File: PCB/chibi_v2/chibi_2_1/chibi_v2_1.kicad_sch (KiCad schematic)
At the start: 12 parts, among them J2 Conn_01x08_Pin, Q1 NPN, Q2 NPN, Q3 NPN

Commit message: PCB update, clearance issues solved (?)
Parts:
- renumbered Display to Display1, Pico to Pico1, SDCard to SDCard1
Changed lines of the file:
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@@
   (symbol (lib_id "components:Adafruit_Micro_SD_SPI_or_SDIO_Card_Breakout_Board") (at 161.29 60.96 0) (unit 1)
     (in_bom yes) (on_board yes) (dnp no) (fields_autoplaced)
-    (property "Reference" "SDCard" (at 184.15 43.18 0)
+    (property "Reference" "SDCard1" (at 184.15 43.18 0)
       (effects (font (size 1.27 1.27)) (justify left))
     )
@@
     (pin "1")
     (instances
-      (project "chibi_v2"
-        (path "/689cf35d-b2ef-4d92-8c34-285453c7ccd9"
-          (reference "SDCard") (unit 1)
+      (project "chibi_v2_1"
+        (path "/689cf35d-b2ef-4d92-8c34-285453c7ccd9"
+          (reference "SDCard1") (unit 1)
         )
       )
@@
     (pin "3")
     (instances
-      (project "chibi_v2"
+      (project "chibi_v2_1"
         (path "/689cf35d-b2ef-4d92-8c34-285453c7ccd9"
           (reference "Q2") (unit 1)
@@
     (pin "1")
     (instances
-      (project "chibi_v2"
+      (project "chibi_v2_1"
         (path "/689cf35d-b2ef-4d92-8c34-285453c7ccd9"
           (reference "#PWR010") (unit 1)
@@
     (pin "2")
     (instances
-      (project "chibi_v2"
+      (project "chibi_v2_1"
         (path "/689cf35d-b2ef-4d92-8c34-285453c7ccd9"
           (reference "R1") (unit 1)
@@
     (pin "1")
     (instances
-      (project "chibi_v2"
+      (project "chibi_v2_1"
         (path "/689cf35d-b2ef-4d92-8c34-285453c7ccd9"
           (reference "#PWR016") (unit 1)
@@
   (symbol (lib_id "SSD1306-128x64_OLED:SSD1306") (at 59.69 74.93 0) (unit 1)
     (in_bom yes) (on_board yes) (dnp no)
-    (property "Reference" "Display" (at 48.26 78.74 90)
+    (property "Reference" "Display1" (at 48.26 78.74 90)
       (effects (font (size 1.27 1.27)) (justify left))
     )
@@
     (pin "2")
     (instances
-      (project "chibi_v2"
-        (path "/689cf35d-b2ef-4d92-8c34-285453c7ccd9"
-          (reference "Display") (unit 1)
+      (project "chibi_v2_1"
+        (path "/689cf35d-b2ef-4d92-8c34-285453c7ccd9"
+          (reference "Display1") (unit 1)
         )
       )
@@
     (pin "2")
     (instances
-      (project "chibi_v2"
+      (project "chibi_v2_1"
         (path "/689cf35d-b2ef-4d92-8c34-285453c7ccd9"
           (reference "R2") (unit 1)
@@
     (pin "1")
     (instances
-      (project "chibi_v2"
+      (project "chibi_v2_1"
         (path "/689cf35d-b2ef-4d92-8c34-285453c7ccd9"
           (reference "#PWR07") (unit 1)
@@
     (pin "3")
     (instances
-      (project "chibi_v2"
+      (project "chibi_v2_1"
         (path "/689cf35d-b2ef-4d92-8c34-285453c7ccd9"
           (reference "Q1") (unit 1)
@@
     (pin "3")
     (instances
-      (project "chibi_v2"
+      (project "chibi_v2_1"
         (path "/689cf35d-b2ef-4d92-8c34-285453c7ccd9"
           (reference "J2") (unit 1)
@@
     (pin "1")
     (instances
-      (project "chibi_v2"
+      (project "chibi_v2_1"
         (path "/689cf35d-b2ef-4d92-8c34-285453c7ccd9"
           (reference "#PWR015") (unit 1)
@@
     (pin "1")
     (instances
-      (project "chibi_v2"
+      (project "chibi_v2_1"
         (path "/689cf35d-b2ef-4d92-8c34-285453c7ccd9"
           (reference "#PWR017") (unit 1)
@@
     (pin "1")
     (instances
-      (project "chibi_v2"
+      (project "chibi_v2_1"
         (path "/689cf35d-b2ef-4d92-8c34-285453c7ccd9"
           (reference "#PWR03") (unit 1)
@@
     (pin "2")
     (instances
-      (project "chibi_v2"
+      (project "chibi_v2_1"
         (path "/689cf35d-b2ef-4d92-8c34-285453c7ccd9"
           (reference "BZ1") (unit 1)
@@
   (symbol (lib_id "MCU_RaspberryPi_and_Boards:Pico") (at 113.03 86.36 0) (unit 1)
     (in_bom yes) (on_board yes) (dnp no) (fields_autoplaced)
-    (property "Reference" "Pico" (at 113.03 54.61 0)
+    (property "Reference" "Pico1" (at 113.03 54.61 0)
       (effects (font (size 1.27 1.27)))
     )
@@
     (pin "17")
     (instances
-      (project "chibi_v2"
-        (path "/689cf35d-b2ef-4d92-8c34-285453c7ccd9"
-          (reference "Pico") (unit 1)
+      (project "chibi_v2_1"
+        (path "/689cf35d-b2ef-4d92-8c34-285453c7ccd9"
+          (reference "Pico1") (unit 1)
         )
       )
@@
     (pin "1")
     (instances
-      (project "chibi_v2"
+      (project "chibi_v2_1"
         (path "/689cf35d-b2ef-4d92-8c34-285453c7ccd9"
           (reference "#PWR014") (unit 1)
@@
     (pin "1")
     (instances
-      (project "chibi_v2"
+      (project "chibi_v2_1"
         (path "/689cf35d-b2ef-4d92-8c34-285453c7ccd9"
           (reference "#PWR012") (unit 1)
@@
     (pin "1")
     (instances
-      (project "chibi_v2"
+      (project "chibi_v2_1"
         (path "/689cf35d-b2ef-4d92-8c34-285453c7ccd9"
           (reference "#PWR06") (unit 1)
@@
     (pin "1")
     (instances
-      (project "chibi_v2"
+      (project "chibi_v2_1"
         (path "/689cf35d-b2ef-4d92-8c34-285453c7ccd9"
           (reference "#PWR04") (unit 1)
@@
     (pin "1")
     (instances
-      (project "chibi_v2"
+      (project "chibi_v2_1"
         (path "/689cf35d-b2ef-4d92-8c34-285453c7ccd9"
           (reference "#PWR01") (unit 1)
@@
     (pin "1")
     (instances
-      (project "chibi_v2"
+      (project "chibi_v2_1"
         (path "/689cf35d-b2ef-4d92-8c34-285453c7ccd9"
           (reference "#PWR05") (unit 1)
@@
     (pin "1")
     (instances
-      (project "chibi_v2"
+      (project "chibi_v2_1"
         (path "/689cf35d-b2ef-4d92-8c34-285453c7ccd9"
           (reference "#PWR08") (unit 1)
@@
     (pin "2")
     (instances
-      (project "chibi_v2"
+      (project "chibi_v2_1"
         (path "/689cf35d-b2ef-4d92-8c34-285453c7ccd9"
           (reference "D1") (unit 1)
@@
     (pin "1")
     (instances
-      (project "chibi_v2"
+      (project "chibi_v2_1"
         (path "/689cf35d-b2ef-4d92-8c34-285453c7ccd9"
           (reference "#PWR013") (unit 1)
@@
     (pin "1")
     (instances
-      (project "chibi_v2"
+      (project "chibi_v2_1"
         (path "/689cf35d-b2ef-4d92-8c34-285453c7ccd9"
           (reference "#PWR011") (unit 1)
@@
     (pin "1")
     (instances
-      (project "chibi_v2"
+      (project "chibi_v2_1"
         (path "/689cf35d-b2ef-4d92-8c34-285453c7ccd9"
           (reference "#PWR09") (unit 1)
@@
     (pin "1")
     (instances
-      (project "chibi_v2"
+      (project "chibi_v2_1"
         (path "/689cf35d-b2ef-4d92-8c34-285453c7ccd9"
           (reference "#PWR02") (unit 1)
@@
     (pin "2")
     (instances
-      (project "chibi_v2"
+      (project "chibi_v2_1"
         (path "/689cf35d-b2ef-4d92-8c34-285453c7ccd9"
           (reference "D2") (unit 1)
@@
     (pin "3")
     (instances
-      (project "chibi_v2"
+      (project "chibi_v2_1"
         (path "/689cf35d-b2ef-4d92-8c34-285453c7ccd9"
           (reference "Q3") (unit 1)

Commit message: charging pins, grb + drl files added
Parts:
- added J1: Conn_01x02, Connector_PinHeader_2.54mm:PinHeader_1x02_P2.54mm_Vertical, symbol Connector_Generic:Conn_01x02
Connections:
- net GND: now also J1.1 (Pin_1)
- net at Pico1.40 (VBUS): now also J1.2 (Pin_2)
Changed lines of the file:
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@@
+    (stroke (width 0) (type default))
+  )
+  (wire (pts (xy 134.62 64.77) (xy 143.51 64.77))
     (stroke (width 0) (type default))
   )
@@
     (stroke (width 0) (type default))
   )
+  (wire (pts (xy 130.81 62.23) (xy 134.62 62.23))
+    (stroke (width 0) (type default))
+  )
   (wire (pts (xy 74.93 74.93) (xy 95.25 74.93))
     (stroke (width 0) (type default))
@@
   )
   (wire (pts (xy 87.63 60.96) (xy 87.63 64.77))
+    (stroke (width 0) (type default))
+  )
+  (wire (pts (xy 134.62 62.23) (xy 134.62 64.77))
     (stroke (width 0) (type default))
   )
@@
     )
   )
+  (symbol (lib_id "Connector_Generic:Conn_01x02") (at 148.59 62.23 0) (unit 1)
+    (in_bom yes) (on_board yes) (dnp no) (fields_autoplaced)
+    (property "Reference" "J1" (at 151.13 62.23 0)
+      (effects (font (size 1.27 1.27)) (justify left))
+    )
+    (property "Value" "Conn_01x02" (at 151.13 64.77 0)
+      (effects (font (size 1.27 1.27)) (justify left))
+    )
+    (property "Footprint" "Connector_PinHeader_2.54mm:PinHeader_1x02_P2.54mm_Vertical" (at 148.59 62.23 0)
+      (effects (font (size 1.27 1.27)) hide)
+    )
+    (property "Datasheet" "~" (at 148.59 62.23 0)
+      (effects (font (size 1.27 1.27)) hide)
+    )
+    (pin "1")
+    (pin "2")
+    (instances
+      (project "chibi_v2_1"
+        (path "/689cf35d-b2ef-4d92-8c34-285453c7ccd9"
+          (reference "J1") (unit 1)
+        )
+      )
+    )
+  )
   (symbol (lib_id "Device:LED") (at 81.28 115.57 180) (unit 1)
     (in_bom yes) (on_board yes) (dnp no) (fields_autoplaced)
@@
         )
       )
+    )
+  )
+  (symbol (lib_id "power:GND") (at 143.51 62.23 270) (unit 1)
+    (in_bom yes) (on_board yes) (dnp no) (fields_autoplaced)
+    (property "Reference" "#PWR018" (at 137.16 62.23 0)
+      (effects (font (size 1.27 1.27)) hide)
+    )
+    (property "Value" "GND" (at 139.7 62.23 90)
+      (effects (font (size 1.27 1.27)) (justify right))
+    )
+    (property "Footprint" "" (at 143.51 62.23 0)
+      (effects (font (size 1.27 1.27)) hide)
+    )
+    (property "Datasheet" "" (at 143.51 62.23 0)
+      (effects (font (size 1.27 1.27)) hide)
+    )
+    (pin "1")
+    (instances
+      (project "chibi_v2_1"
+        (path "/689cf35d-b2ef-4d92-8c34-285453c7ccd9"
+          (reference "#PWR018") (unit 1)
+        )
+      )

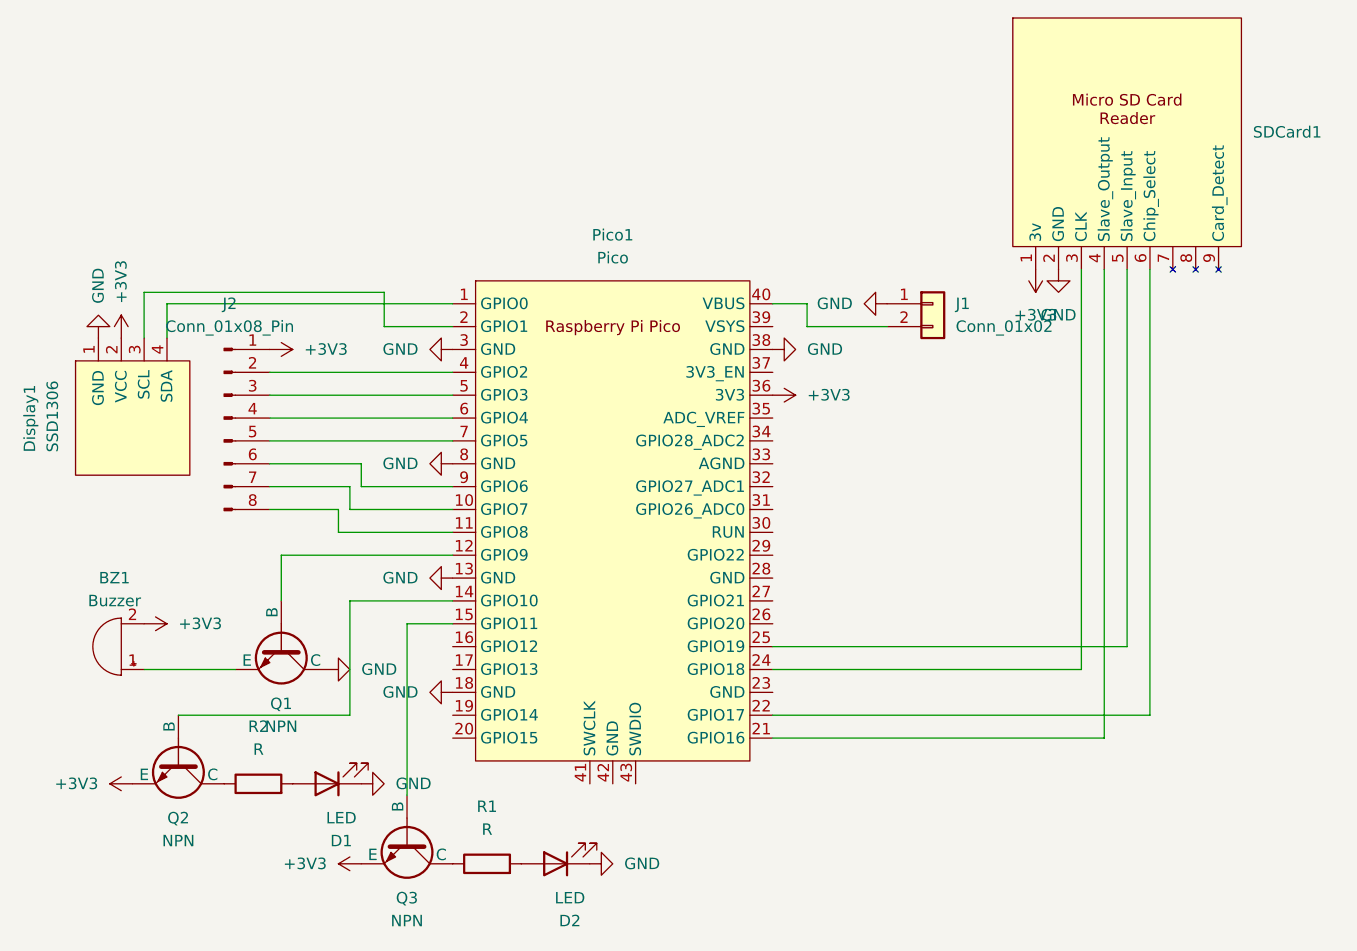
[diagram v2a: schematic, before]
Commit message: repositioning of a few components in PCB V2.1
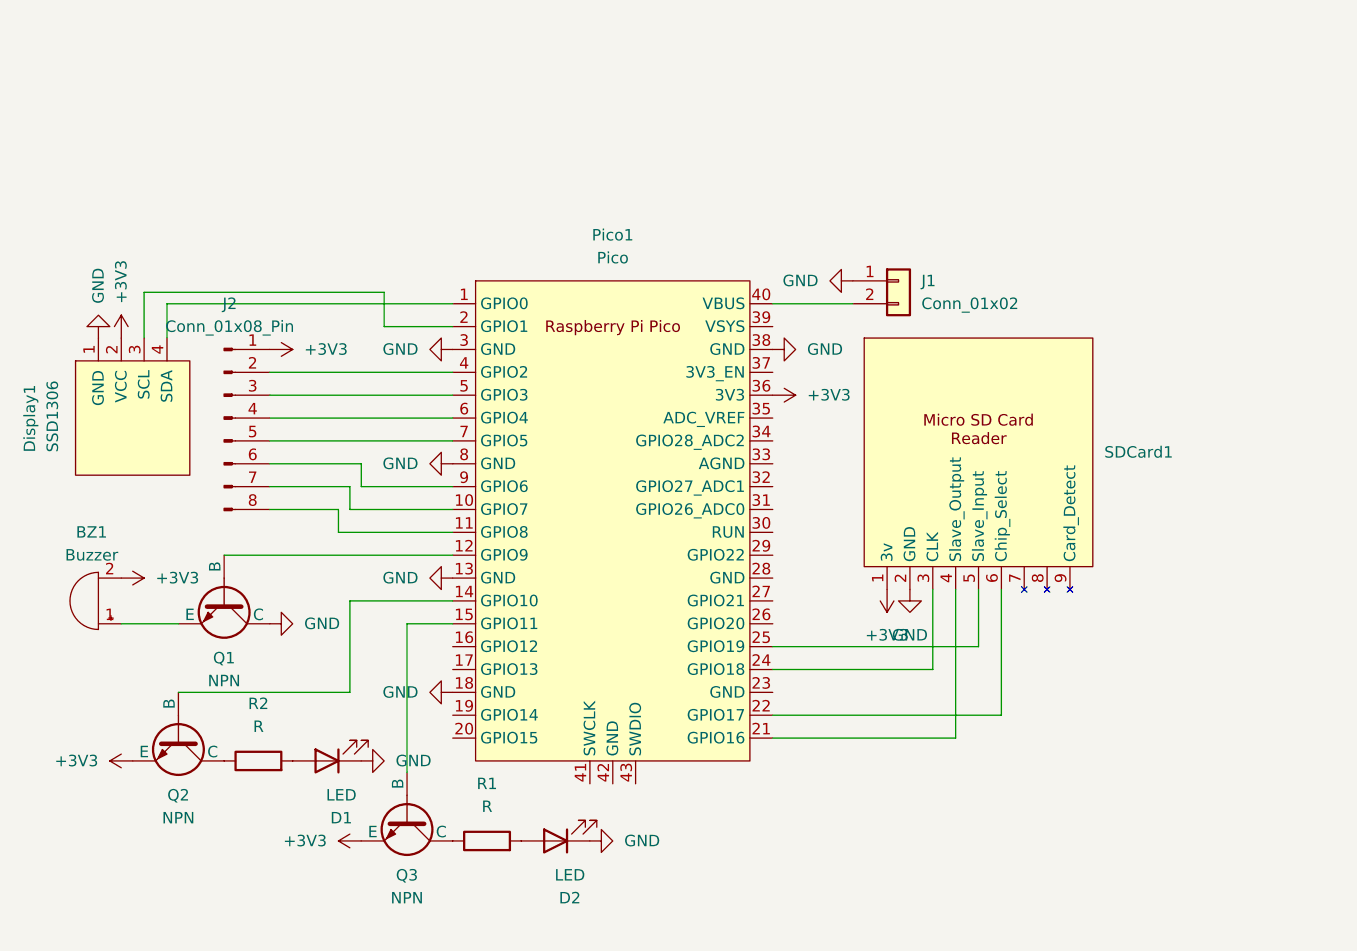
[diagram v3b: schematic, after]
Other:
- moved on the sheet: BZ1, D1, D2, J1, Q1, Q2, Q3, R1, R2, SDCard1
